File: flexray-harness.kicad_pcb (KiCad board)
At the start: 2 copper layers, 57 x 70 mm, 64 parts, among them J2 CAN, J3 POWER, J4 FR1, J5 FR2, J6 USB_C_Receptacle, K2 G6K-2, U1 NCV7383, U2 ATA6561-GAQW-N, U3 NCV7383, U6 MCP2518FDT-E/QBB, U9 TPS54302, Y1 ABM8G-40.000MHZ-4Y-T3

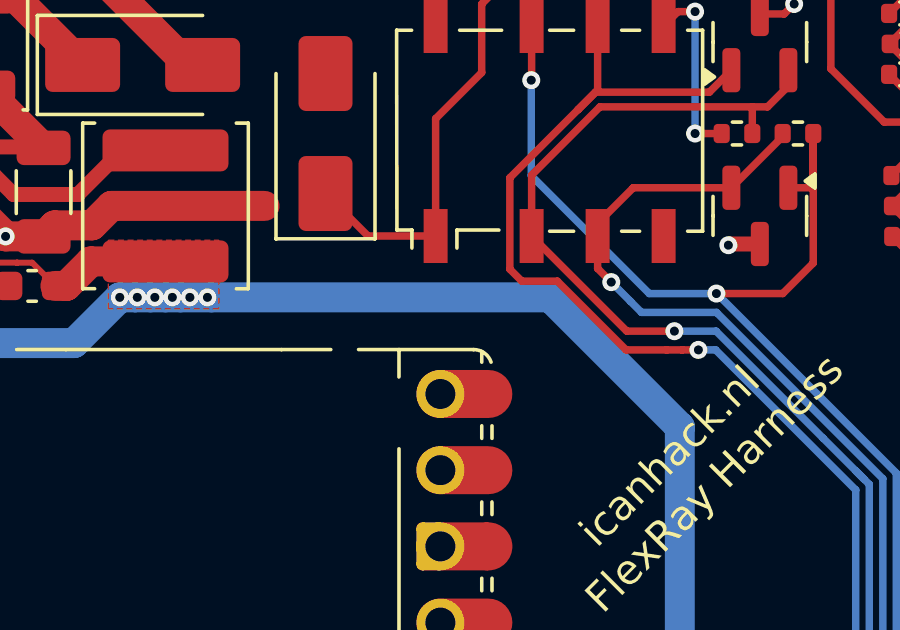
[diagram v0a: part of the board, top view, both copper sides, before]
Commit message: connect relay pin to GPIO
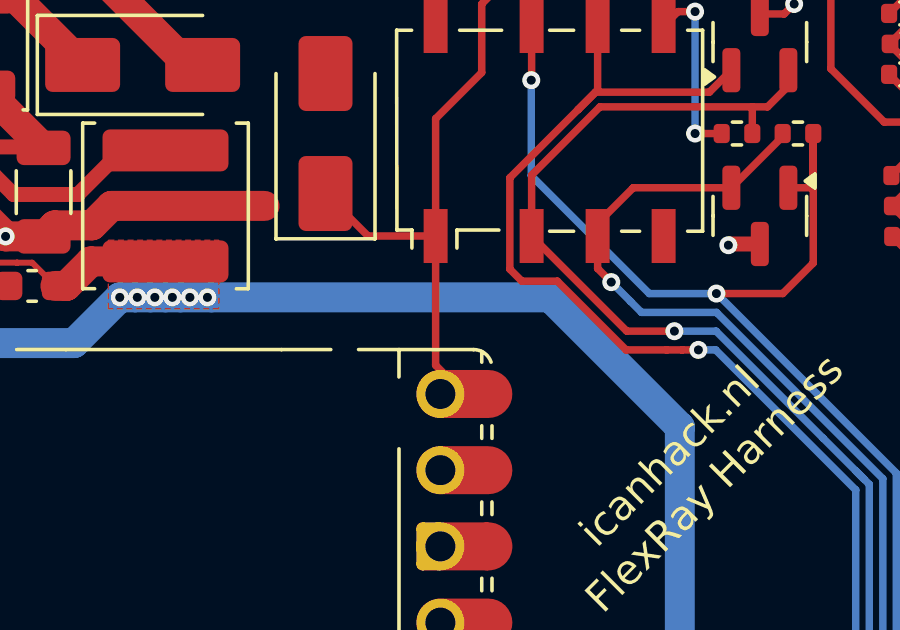
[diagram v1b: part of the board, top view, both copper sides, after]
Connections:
- A1 pad 20: unconnected-(A1-GPIO15-Pad20)_1 -> /RELAY
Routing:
- net /RELAY: track 40.6 -> 46.5 mm
